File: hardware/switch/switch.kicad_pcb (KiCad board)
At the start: 2 copper layers, 70.5 x 70.5 mm, 31 parts, among them J1 Conn_01x07, J2 Conn_01x04, J3 Conn_01x04, J4 Conn_01x04, K1 G6SU-2, K2 G6SU-2, K3 G6SU-2, K4 G6SU-2, SW1 D2F-01, SW2 D2F-01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

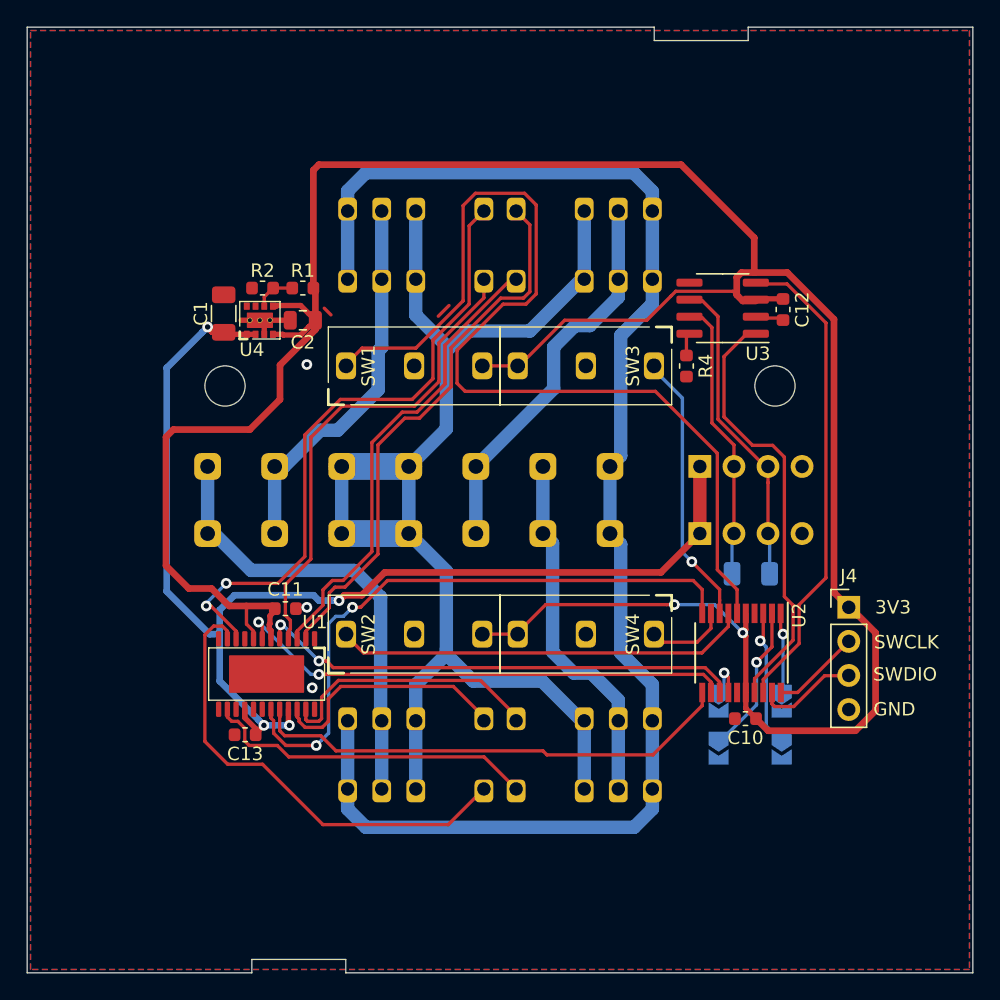
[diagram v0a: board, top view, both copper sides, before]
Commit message: Use LIN instead of CAN transciever
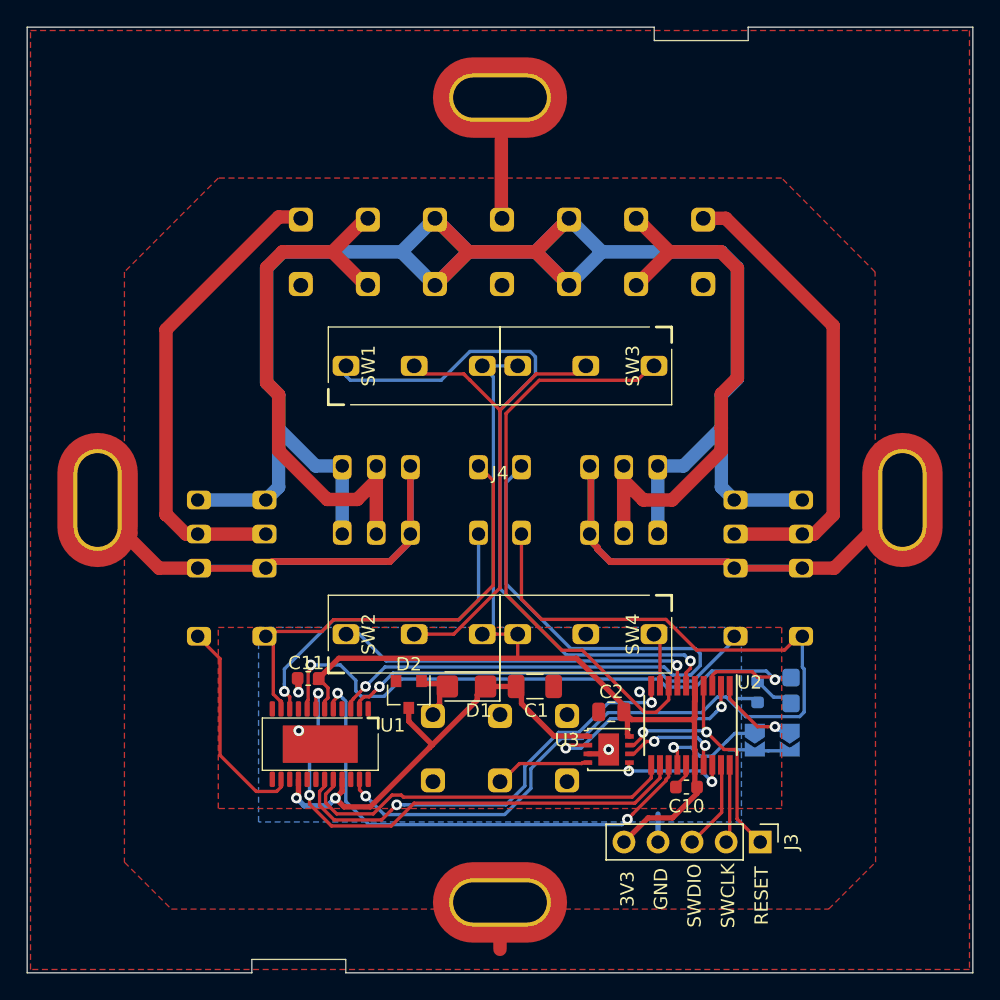
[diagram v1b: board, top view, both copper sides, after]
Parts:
- removed C12, C13: C, Capacitor_SMD:C_0603_1608Metric
- removed JP3, JP4: SolderJumper_2_Open, Jumper:SolderJumper-2_P1.3mm_Open_TrianglePad1.0x1.5mm
- removed R2: 10k, Resistor_SMD:R_0603_1608Metric
- removed R3: 120R, Resistor_SMD:R_1206_3216Metric
- removed R4: 100k, Resistor_SMD:R_0603_1608Metric
- removed REF**: Switch_Mount, RoomControl:Switch_Mount
- removed U4: TPS82130, RoomControl:Texas_TPS82130
- added D1: D, Diode_SMD:D_1206_3216Metric_Castellated, F.Cu at (97.5, 113.9)
- added D2: D, Diode_SMD:D_SOT-23_ANK, F.Cu at (93.2, 114.5)
- added D3: LED, LED_SMD:LED_0805_2012Metric_Castellated, B.Cu at (121.7, 114.2)
- J2: value Conn_01x04 -> Conn_01x03; footprint Connector_PinHeader_2.54mm:PinHeader_1x04_P2.54mm_Vertical -> RoomControl:Wago_236-403
- J3: value Conn_01x04 -> Conn_01x05; footprint Connector_PinHeader_2.54mm:PinHeader_1x04_P2.54mm_Vertical -> Connector_PinHeader_2.54mm:PinHeader_1x05_P2.54mm_Vertical; moved to F.Cu
- J4: footprint Connector_PinHeader_2.54mm:PinHeader_1x04_P2.54mm_Vertical -> RoomControl:Switch_Mount
- R1: value 33k -> 330R; moved to B.Cu
- U1: value NCV7726B -> NCV7718CDQR2G; footprint RoomControl:On_NCV7726B -> RoomControl:On_NCV77xx
- U3: value SN65HVD230 -> NCV7428MW3; footprint Package_SO:SOIC-8_3.9x4.9mm_P1.27mm -> Package_DFN_QFN:DFN-8-1EP_3x3mm_P0.65mm_EP1.55x2.4mm
- moved R1 45.3 mm to (119.2, 114.3), turned to 270 degrees
- moved C2 37.2 mm to (108.3, 115.8)
- moved C1 36.2 mm to (102.6, 113.9), turned to 0 degrees
- moved U3 34.0 mm to (108.1, 118.6), turned to 0 degrees
- moved J1 29.6 mm to (85.2, 81.5), turned to 270 degrees
- moved J3 28.4 mm to (119.4, 125.5)
- moved J4 27.2 mm to (100.0, 100.0)
- moved J2 25.5 mm to (95.0, 118.5)
- moved K2 20.8 mm to (80.0, 110.2), turned to 0 degrees
- moved K4 20.8 mm to (120.0, 110.2), turned to 0 degrees
- moved K1 19.0 mm to (98.4, 100.0)
- moved K3 19.0 mm to (101.6, 100.0)
- moved C10 6.74 mm to (113.9, 121.4)
- moved U2 6.60 mm to (114.2, 116.8)
- moved U1 6.58 mm to (86.6, 118.2)
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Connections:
- net JPA0 renamed JPA
- net SPI_MISO renamed HB_MISO
- net SPI_MOSI renamed HB_MOSI
- net SPI_SCK renamed HB_SCK
- net SPI_SS renamed HB_SS
- J1 pad 1: PE -> KA1
- J1 pad 2: KB1 -> KA0
- J1 pad 3: KB0 -> L
- J1 pad 4: L -> PE
- J1 pad 6: KA0 -> KB0
- J1 pad 7: KA1 -> KB1
- J2 pad 1: +12V -> Net-(D1-Pad2)
- J2 pad 2: CANH -> LIN
- J2 pad 3: CANL -> GND
- J3 pad 1: +12V -> RESET
- J3 pad 2: CANH -> SWCLK
- J3 pad 3: CANL -> SWDIO
- J4 pad 1: +3V3 -> PE
- J4 pad 2: SWCLK -> PE
- J4 pad 3: SWDIO -> PE
- J4 pad 4: GND -> PE
- JP2 pad 1: JPA1 -> JPB
- K1 pad 10: L -> PE
- K1 pad 3: L -> PE
- K1 pad 5: PE -> L
- K1 pad 8: PE -> L
- K2 pad 10: L -> PE
- K2 pad 12: HB4 -> HB2
- K2 pad 3: L -> PE
- K2 pad 5: PE -> L
- K2 pad 8: PE -> L
- K3 pad 1: HB5 -> HB4
- K3 pad 10: L -> PE
- K3 pad 12: HB6 -> HB5
- K3 pad 3: L -> PE
- K3 pad 5: PE -> L
- K3 pad 8: PE -> L
- K4 pad 1: HB7 -> HB6
- K4 pad 10: L -> PE
- K4 pad 12: HB8 -> HB5
- K4 pad 3: L -> PE
- K4 pad 5: PE -> L
- K4 pad 8: PE -> L
- R1 pad 1: +3V3 -> Net-(D3-Pad1)
- R1 pad 2: Net-(R1-Pad2) -> GND
- U1 pad 1: GND -> Net-(U1-Pad1)
- U1 pad 10: HB2 -> HB1
- U1 pad 11: HB3 -> HB2
- U1 pad 12: GND -> Net-(U1-Pad12)
- U1 pad 14: HB8 -> HB3
- U1 pad 2: HB5 -> HB6
- U1 pad 22: HB4 -> Net-(U1-Pad22)
- U1 pad 23: HB7 -> HB5
- U1 pad 3: HB6 -> HB4
- U1 pad 4: HB1 -> Net-(U1-Pad4)
- U1 pad 8: +3V3 -> HB_EN
- U2 pad 1: JPB0 -> JPB
- U2 pad 17: TX -> LIN_TX
- U2 pad 18: RX -> LIN_RX
- U2 pad 2: JPA1 -> LIN_EN
- U2 pad 3: JPB1 -> HB_EN
- U2 pad 4: Net-(U2-Pad4) -> RESET
- U3 pad 1: TX -> +12V
- U3 pad 2: GND -> LIN_EN
- U3 pad 3: +3V3 -> GND
- U3 pad 4: RX -> LIN
- U3 pad 5: Net-(U3-Pad5) -> LIN_RX
- U3 pad 6: CANL -> LIN_TX
- U3 pad 7: CANH -> RESET
- U3 pad 8: Net-(R4-Pad1) -> +3V3
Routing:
- net +3V3: track 203.8 -> 81.0 mm, vias 2 -> 0
- net +12V: track 89.9 -> 35.0 mm, vias 4 -> 2
- net HB_EN: track 0.00 -> 48.1 mm, vias 0 -> 2
- net L: track 97.3 -> 142.0 mm
- net GND: track 8.02 -> 49.7 mm, vias 3 -> 4
- net HB4: track 18.4 -> 55.0 mm, vias 0 -> 1
- net RX: track 35.9 -> 0.00 mm
- net TX: track 32.5 -> 0.00 mm
- net HB5: track 41.3 -> 73.4 mm, vias 0 -> 1
- net HB8: track 24.9 -> 0.00 mm
- net CANL: track 23.5 -> 0.00 mm
- net SWB0: track 20.5 -> 43.2 mm, vias 1 -> 0
- net SWA0: track 75.0 -> 52.9 mm, vias 0 -> 1
- net CANH: track 20.7 -> 0.00 mm
- net RESET: track 0.00 -> 20.3 mm, vias 0 -> 2
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- added copper zone on F.Cu, net PE
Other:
- net class HiVolt removed
- net class Mains added: clearance 1, trace_width 0.25, via_dia 0.8, via_drill 0.4
- net class PE removed
- board text added: "RESET"

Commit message: Update main board to use LIN
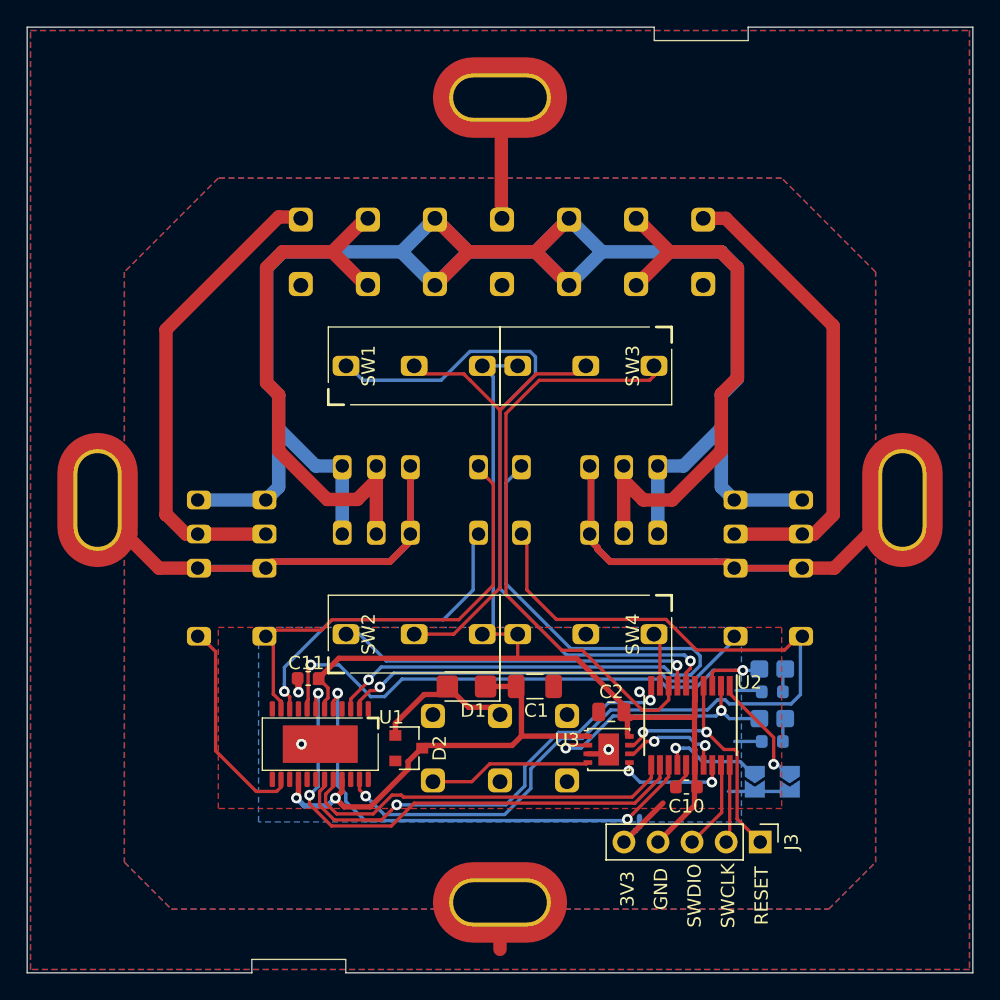
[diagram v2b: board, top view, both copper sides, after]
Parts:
- added D4: LED, LED_SMD:LED_0805_2012Metric_Castellated, B.Cu at (120.3, 112.6)
- added R2: 330R, Resistor_SMD:R_0603_1608Metric, B.Cu at (120.3, 114.3)
- JP1, JP2: footprint Jumper:SolderJumper-2_P1.3mm_Open_TrianglePad1.0x1.5mm -> RoomControl:Jumper2Triangular
- moved D2 4.00 mm to (93.2, 118.5), turned to 0 degrees
- moved R1 3.86 mm to (120.3, 118.0), turned to 180 degrees
- moved JP1 3.10 mm to (119.0, 121.0)
- moved JP2 3.10 mm to (121.6, 121.0)
- moved D3 2.52 mm to (120.3, 116.3), turned to 180 degrees
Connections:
- net HB1 renamed AX
- net HB2 renamed AY
- net HB3 renamed AZ
- net HB4 renamed BX
- net HB5 renamed BY
- net HB6 renamed BZ
- D3 pad 2: HB_EN -> LIN_EN
- J2 pad 1: Net-(D1-Pad2) -> LIN
- J2 pad 2: LIN -> Net-(D1-Pad2)
- J3 pad 4: GND -> +3V3
- J3 pad 5: +3V3 -> GND
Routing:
- net Net-(D1-Pad2): track 4.64 -> 11.7 mm
- net GND: track 49.7 -> 56.3 mm
- net HB_EN: track 48.1 -> 42.5 mm
- net LIN: track 7.30 -> 12.5 mm
- net LIN_EN: track 16.2 -> 19.4 mm
- net BY: track 73.4 -> 70.8 mm
- net JPB: track 6.42 -> 8.66 mm
- net +3V3: track 81.0 -> 79.0 mm
- net Net-(D4-Pad1): track 0.00 -> 1.77 mm
- net Net-(D3-Pad1): track 3.18 -> 1.77 mm
- net +12V: track 35.0 -> 34.2 mm
- net AX: track 24.7 -> 24.1 mm
- net JPA: track 8.55 -> 7.96 mm
- added copper zone on B.Cu, net PE
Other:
- board text added: "12V"
- board text added: "LIN"

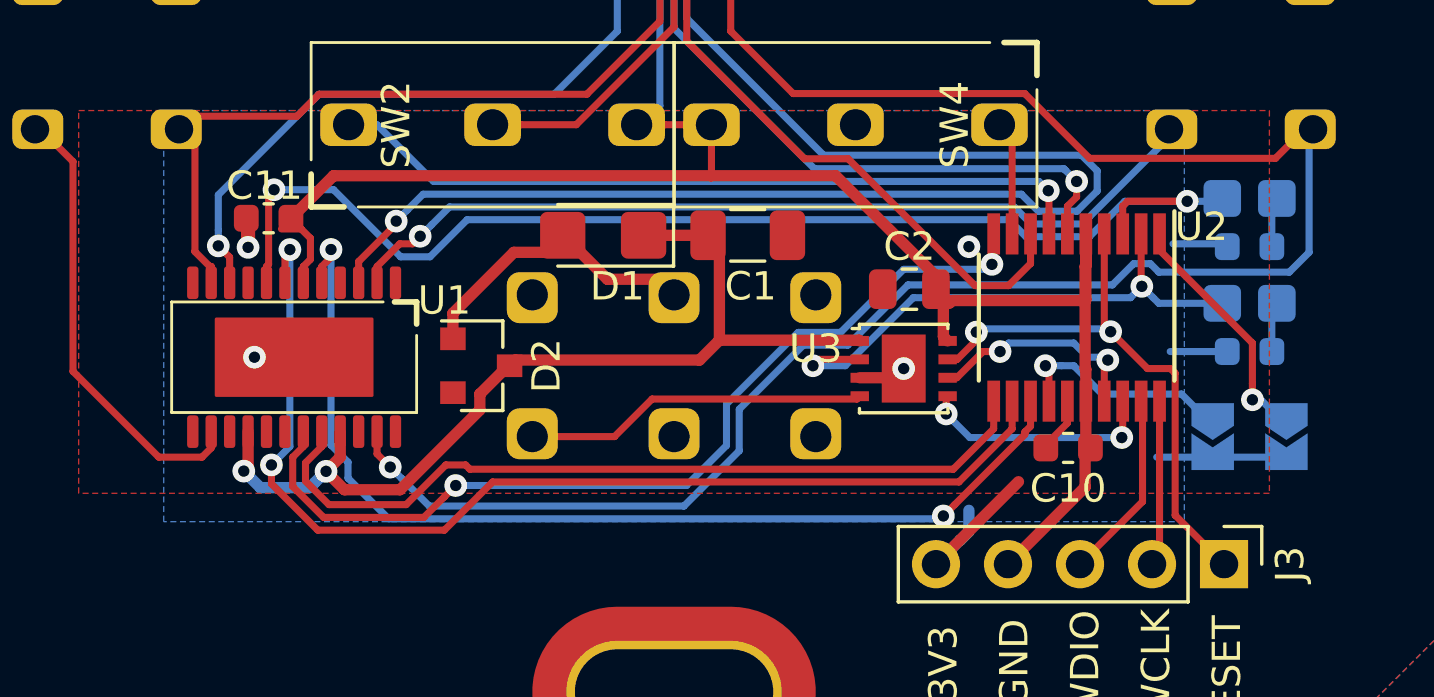
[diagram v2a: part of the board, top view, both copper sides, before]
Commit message: Add backup battery and 32768Hz crystal
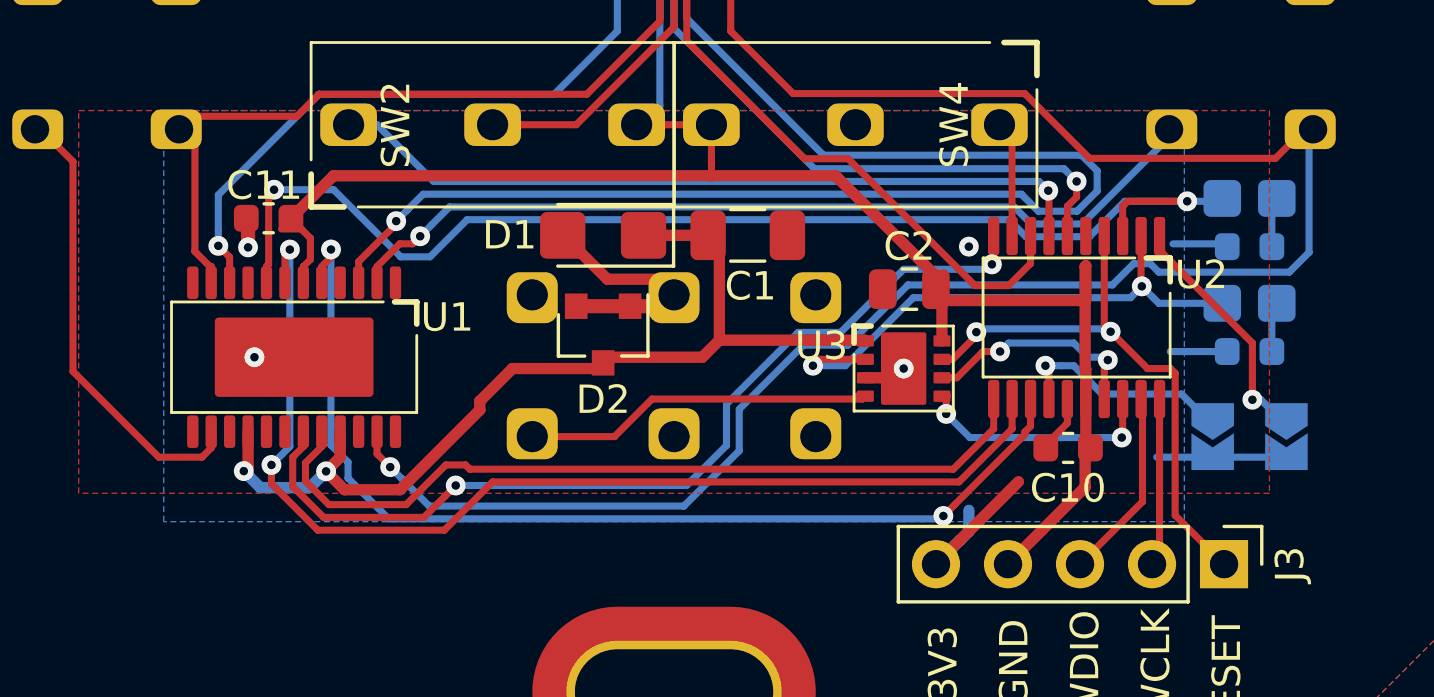
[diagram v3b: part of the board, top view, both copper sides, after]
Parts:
- C1: value 10u/25V/7XR -> 10u/25V/X7R
- C10, C11: value C -> 100n
- C2: value 22u -> 22u/16V
- D2: value D -> BAS40-05/BAT54C; footprint Diode_SMD:D_SOT-23_ANK -> Package_TO_SOT_SMD:SOT-23
- JP1, JP2: footprint RoomControl:Jumper2Triangular -> RoomControl:Jumper2
- U2: footprint Package_SO:TSSOP-20_4.4x6.5mm_P0.65mm -> RoomControl:STM32F042F6
- U3: footprint Package_DFN_QFN:DFN-8-1EP_3x3mm_P0.65mm_EP1.55x2.4mm -> RoomControl:On_NCV7428MW
- moved D2 4.44 mm to (97.5, 117.4), turned to 270 degrees
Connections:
- D2 pad 1: +12V -> Net-(D1-Pad2)
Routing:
- net +3V3: track 79.0 -> 76.6 mm
- net Net-(D1-Pad2): track 11.7 -> 9.46 mm
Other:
- net class Default: via_dia 0.8 -> 0.7; via_drill 0.4 -> 0.3

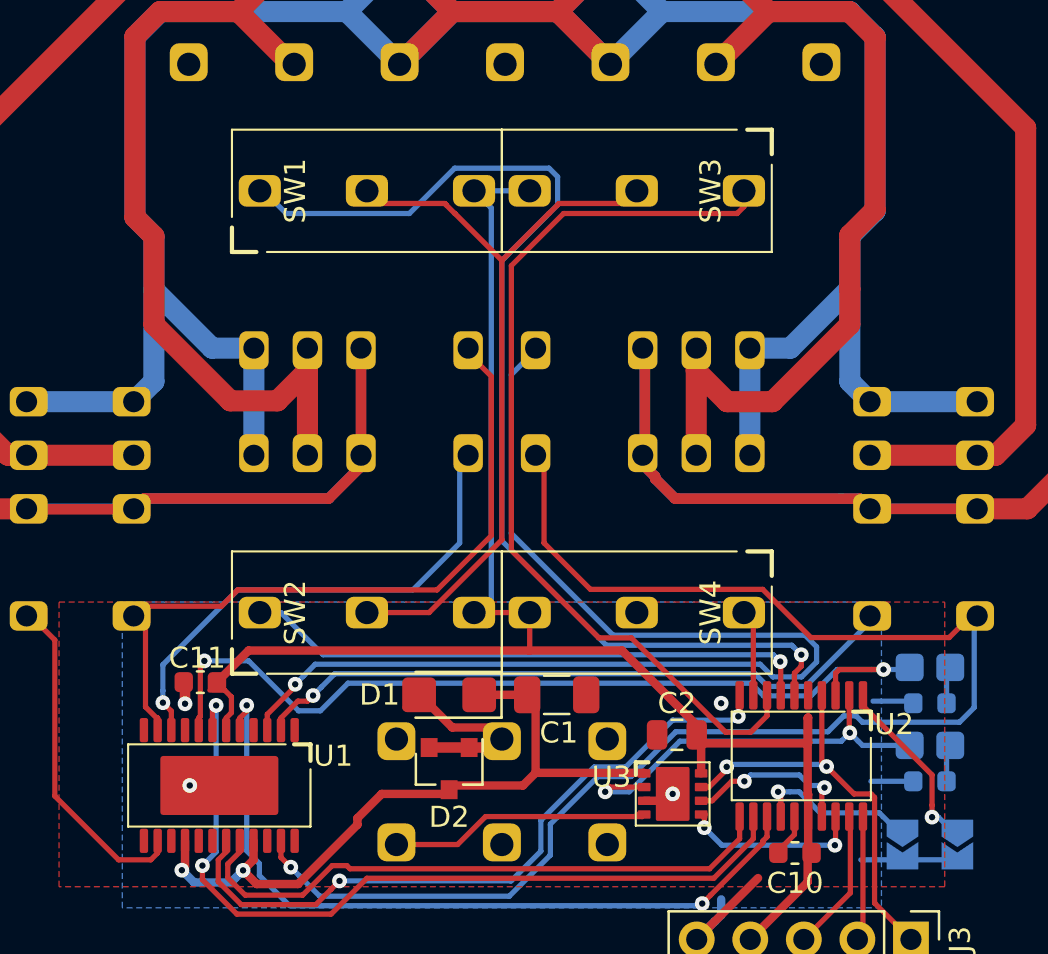
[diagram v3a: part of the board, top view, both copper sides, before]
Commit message: New speaker and pir sensor lens
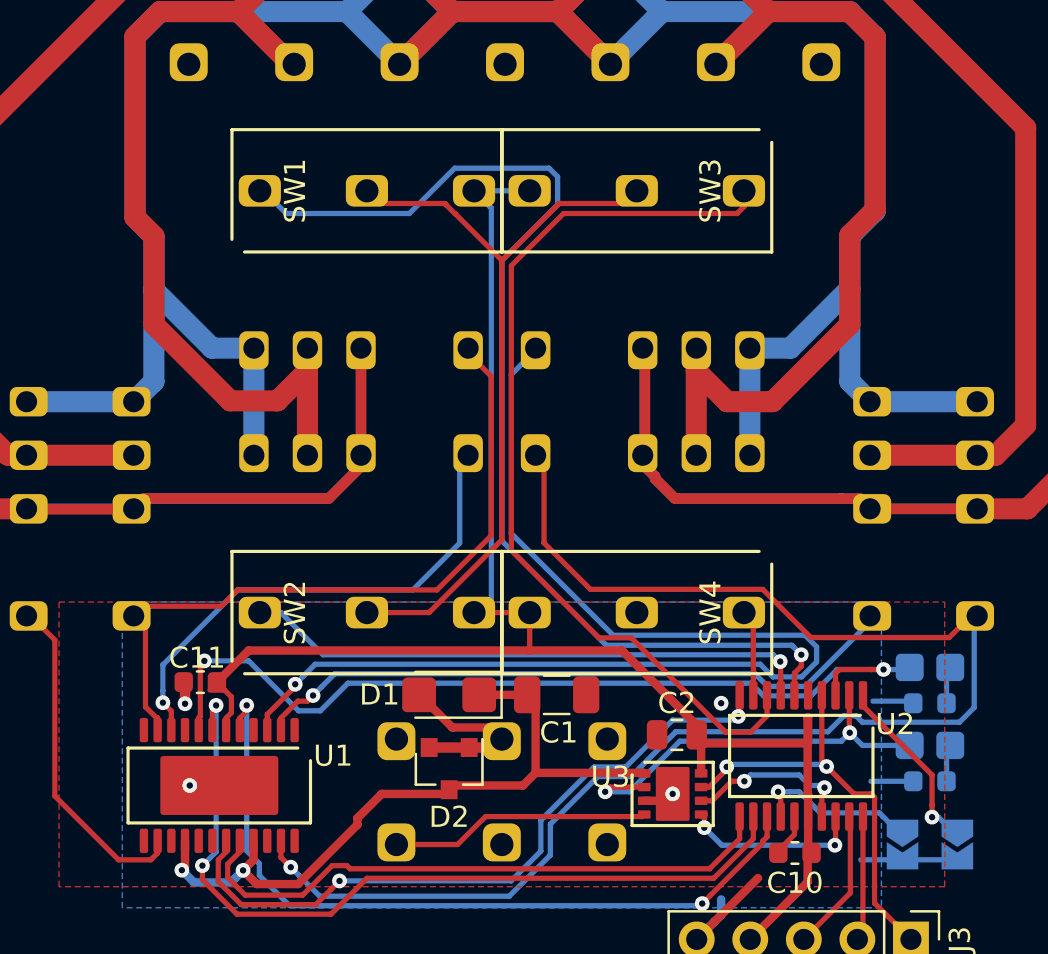
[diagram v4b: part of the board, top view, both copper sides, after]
